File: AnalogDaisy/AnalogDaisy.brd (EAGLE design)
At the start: 58.1 x 43.2 mm, 21 parts, among them J1 1X2-3.5MM, J2 1X2-3.5MM, J3 1X2-3.5MM, J4 1X2-3.5MM, J5 1X2-3.5MM, J7 POWER_JACKPTH_BREAD, Q1 35A/25V/8.5mΩ, Q3 35A/25V/8.5mΩ, Q5 35A/25V/8.5mΩ, Q6 35A/25V/8.5mΩ

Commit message: moved inductor, git test
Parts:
- moved L1 24.1 mm to (8.89, 6.35)
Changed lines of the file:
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@@
 <?xml version="1.0" encoding="utf-8"?>
 <!DOCTYPE eagle SYSTEM "eagle.dtd">
-<eagle version="8.4.3">
+<eagle version="8.2.2">
 <drawing>
 <settings>
@@
 <param name="dpMaxLengthDifference" value="10mm"/>
 <param name="dpGapFactor" value="2.5"/>
+<param name="checkGrid" value="0"/>
 <param name="checkAngle" value="0"/>
 <param name="checkFont" value="1"/>
 <param name="checkRestrict" value="1"/>
-<param name="checkStop" value="0"/>
 <param name="useDiameter" value="13"/>
 <param name="maxErrors" value="50"/>
@@
 <element name="C12" library="microbuilder" package="0603-MINI" value="22uF 10V" x="6.35" y="-31.75"/>
 <element name="C13" library="microbuilder" package="0603-MINI" value="22uF 10V" x="-1.27" y="-34.29"/>
-<element name="L1" library="microbuilder" package="INDUCTOR_5X5MM_TDK_VLC5045" value="4.7uH" x="1.27" y="-16.51"/>
+<element name="L1" library="microbuilder" package="INDUCTOR_5X5MM_TDK_VLC5045" value="4.7uH" x="8.89" y="6.35"/>
 <element name="C14" library="microbuilder" package="0603-MINI" value="22nF" x="6.35" y="-34.29"/>
 <element name="D6" library="microbuilder" package="SOD-123" value="PMEG4030ER" x="-1.27" y="-27.94"/>
@@
 <contactref element="U$19" pad="P5"/>
 <wire x1="5.6" y1="-31.75" x2="-2.02" y2="-34.29" width="0" layer="19" extent="1-1"/>
-<wire x1="2.87" y1="-16.51" x2="5.6" y2="-31.75" width="0" layer="19" extent="1-1"/>
-<wire x1="6.87" y1="-12.88" x2="2.87" y2="-16.51" width="0" layer="19" extent="1-1"/>
+<wire x1="10.49" y1="6.35" x2="5.6" y2="-31.75" width="0" layer="19" extent="1-1"/>
+<wire x1="6.87" y1="-12.88" x2="10.49" y2="6.35" width="0" layer="19" extent="1-1"/>
 <wire x1="12.7" y1="12.7" x2="6.87" y2="-12.88" width="0" layer="19" extent="1-16"/>
 </signal>
@@
 <contactref element="U$19" pad="P13"/>
 <contactref element="D6" pad="C"/>
-<wire x1="-0.33" y1="-16.51" x2="-3.12" y2="-27.94" width="0" layer="19" extent="1-1"/>
-<wire x1="6.17" y1="-10.68" x2="-0.33" y2="-16.51" width="0" layer="19" extent="1-1"/>
+<wire x1="7.29" y1="6.35" x2="-3.12" y2="-27.94" width="0" layer="19" extent="1-1"/>
+<wire x1="6.17" y1="-10.68" x2="7.29" y2="6.35" width="0" layer="19" extent="1-1"/>
 <wire x1="6.87" y1="-9.98" x2="6.17" y2="-10.68" width="0" layer="19" extent="1-1"/>
 <wire x1="8.37" y1="-9.98" x2="6.87" y2="-9.98" width="0" layer="19" extent="1-1"/>
@@
 <compatibility>
 <note version="8.2" severity="warning">
-Since Version 8.2, EAGLE supports online libraries. The ids
+Since Version 8.2, Eagle supports online libraries. The ids
 of those online libraries will not be understood (or retained)
 with this version.

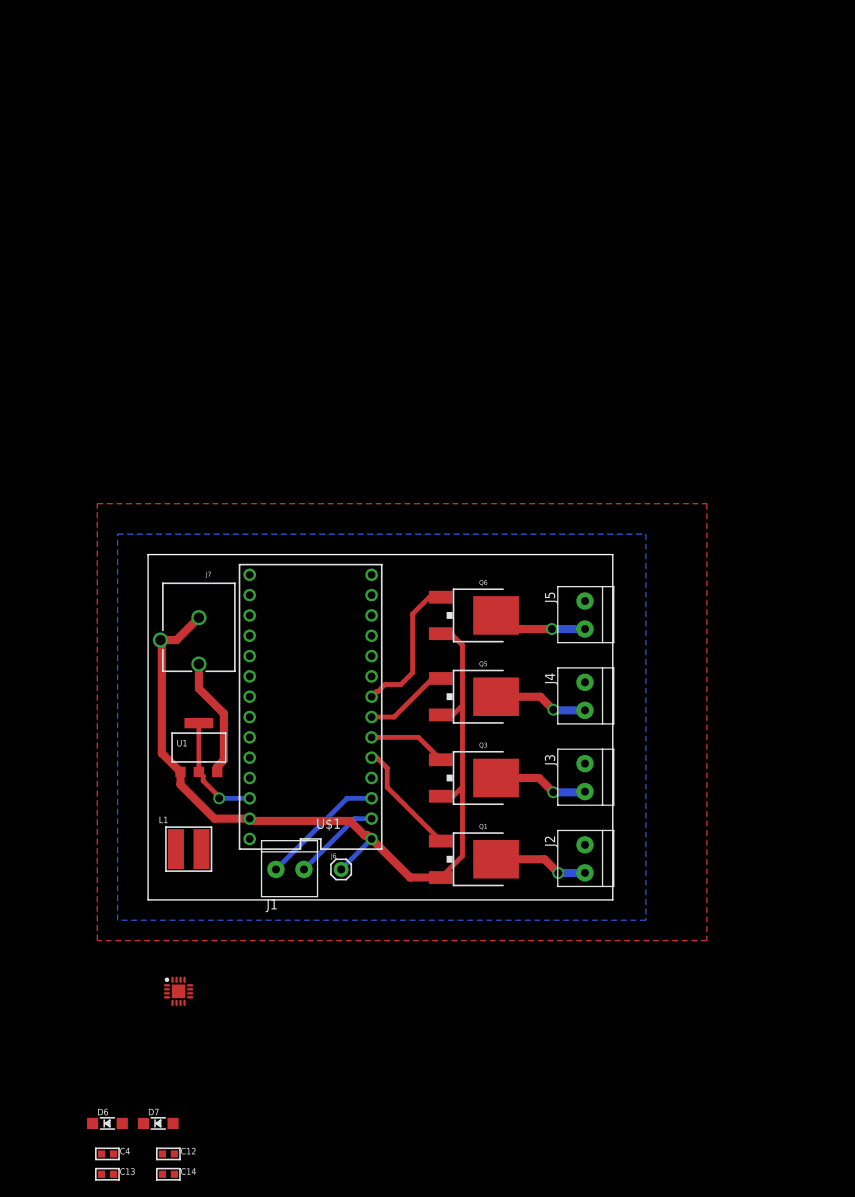
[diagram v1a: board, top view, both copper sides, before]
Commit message: Updated AnalogDaisy
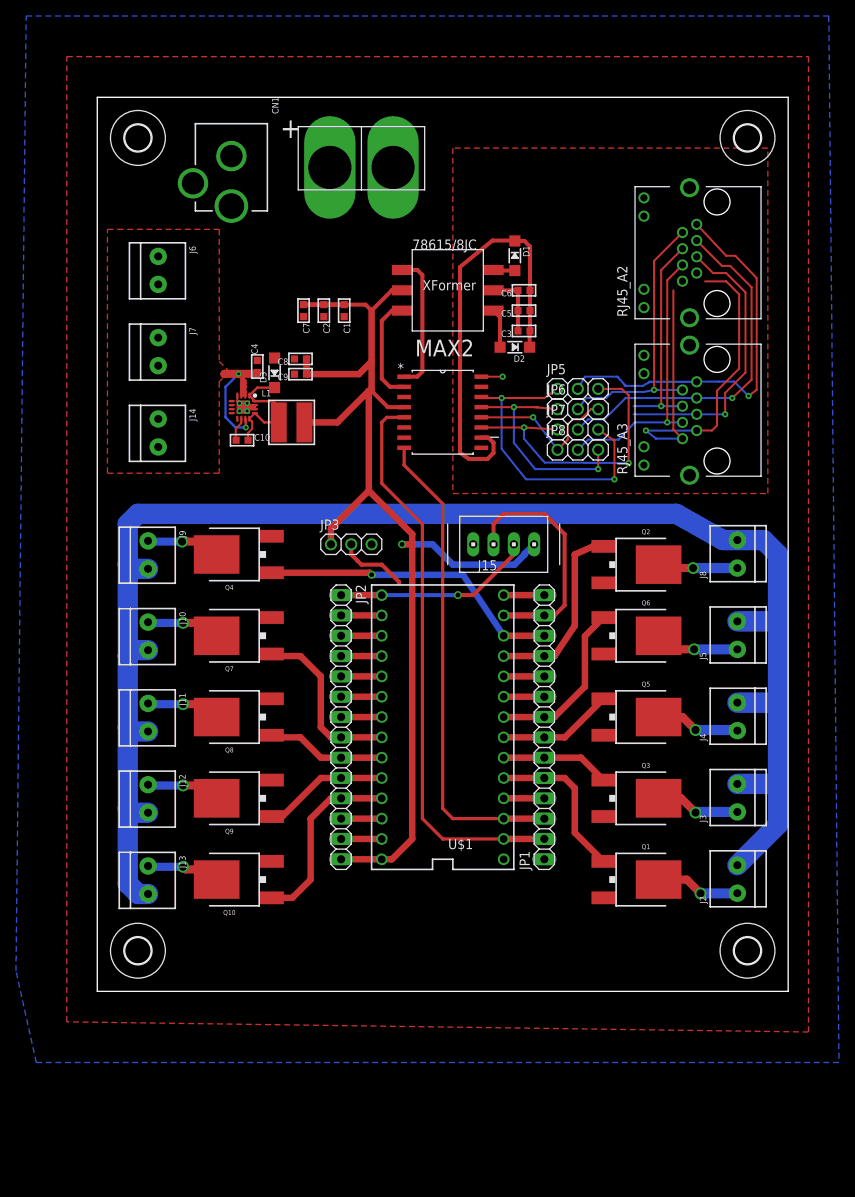
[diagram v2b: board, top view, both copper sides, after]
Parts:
- removed C12, C13: 22uF 10V, microbuilder:0603-MINI
- removed C14: 22nF, microbuilder:0603-MINI
- removed D6, D7: PMEG4030ER, microbuilder:SOD-123
- removed U1: (no value), microbuilder:SOT223-R
- added C1, C5: 1uF 10V, microbuilder:0603-MINI
- added C10: 22nF, microbuilder:0603-MINI
- added C2, C6: 0.1uF 10V, microbuilder:0603-MINI
- added C3, C7: 10uF 10V, microbuilder:0603-MINI
- added C8, C9: 22uF 10V, microbuilder:0603-MINI
- added CN1: (no value), microbuilder:DCJACK_2MM_PTH
- added D1, D2, D3: PMEG4030ER, microbuilder:SOD-123
- added J10, J11, J12, J13, J14, J8, J9: (no value), microbuilder:TERMBLOCK_1X2-3.5MM
- added J15: (no value), My Connectors:BOARDMOUNT-LED
- added JP1, JP2: (no value), adafruit:1X14
- added JP3, JP5, JP6, JP7, JP8: (no value), adafruit:1X03
- added MAX2: MAX14853GWE+, Maxim_By_element14_Batch_1:SOIC127P1034X267-16N
- added Q10, Q2, Q4, Q7, Q8, Q9: 35A/25V/8.5mΩ, SparkFun-DiscreteSemi:DPAK
- added RJ45_A2, RJ45_A3: RJHSE-5381, RJHSE-5381:AMPHENOL_RJHSE-5381
- added U$11, U$15, U$16: (no value), holes:3,3
- added U$2: BUCK_CONVERTER, Heep:QFN-16
- added XFORM2: 78615/8JC, trafo-murata:0.1_SMD
- J1: value 1X2-3.5MM -> POWERPOLE_POWER45A_DRILL; device adafruit:1X2-3.5MM -> powerpoles:POWERPOLE_PAIR_45A_HOLE
- J2, J3, J4, J5: value 1X2-3.5MM -> (none); device adafruit:1X2-3.5MM -> microbuilder:TERMBLOCK_1X2-3.5MM
- J6: device SparkFun-Connectors:1X01 -> microbuilder:TERMBLOCK_1X2-3.5MM
- J7: value POWER_JACKPTH_BREAD -> (none); device SparkFun-Connectors:POWER_JACK_PTH_BREAD -> microbuilder:TERMBLOCK_1X2-3.5MM
- U$19: value BUCK_CONVERTER -> (none); device Heep:QFN-16 -> holes:3,3
- moved C4 100.2 mm to (17.5, 66.7), turned to 90 degrees
- moved J1 89.3 mm to (30.5, 92.7), turned to 0 degrees
- moved J6 78.3 mm to (5.08, 78.7), turned to 270 degrees
- moved U$19 71.3 mm to (78.7, -6.35)
- moved L1 54.9 mm to (21.7, 59.7)
- moved J7 25.9 mm to (5.08, 68.6), turned to 270 degrees
- moved Q1 20.5 mm to (66.0, 2.54)
- moved Q3 20.5 mm to (66.0, 12.7)
- moved Q5 20.5 mm to (66.0, 22.9)
- moved Q6 20.5 mm to (66.0, 33.0)
- moved J2 19.2 mm to (77.5, 2.54)
- moved J3 19.2 mm to (77.5, 12.7)
- moved J4 19.2 mm to (77.5, 22.9)
- moved J5 19.2 mm to (77.5, 33.0)
- moved U$1 16.7 mm to (40.6, 21.6)
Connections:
- removed net +3V3: C12.1, C13.1, L1.P$2, U$1.3.3V, U$19.P5, U1.2, U1.4
- removed net VBUS: D7.A
- removed net VIN: U$1.VIN
- new net +3V1: U$2.P5
- new net +5V: C1.1, C2.1, C7.1, C9.1, J15.1, JP2.14, JP3.1, L1.P$2, MAX2.4, U$1.VIN, XFORM2.PIN2
- new net APA_CLOCK: J15.2, JP2.1, U$1.13
- new net APA_DATA: J15.3, JP1.13, U$1.11
- new net DRAIN10: J13.2, Q10.4
- new net DRAIN5: J8.2, Q2.4
- new net DRAIN6: J9.2, Q4.4
- new net DRAIN7: J10.2, Q7.4
- new net DRAIN8: J11.2, Q8.4
- new net DRAIN9: J12.2, Q9.4
- new net EN10: JP2.11, Q10.1, U$1.23/A9
- new net EN5: JP1.11, Q2.1, U$1.9
- new net EN6: JP1.12, Q4.1, U$1.10
- new net EN7: JP2.8, Q7.1, U$1.20/A6
- new net EN8: JP2.9, Q8.1, U$1.21/A7
- new net EN9: JP2.10, Q9.1, U$1.22/A8
- new net GNDB: C3.2, C5.2, C6.2, MAX2.15, MAX2.9, RJ45_A2.7, RJ45_A2.8, RJ45_A2.S1, RJ45_A2.S2, RJ45_A3.7, RJ45_A3.8, XFORM2.PIN5
- new net GNDBREAK: CN1.GNDBREAK
- new net N$10: JP1.14, U$1.12
- new net N$12: JP2.2, U$1.14/A0
- new net N$13: JP2.3, U$1.15/A1
- new net N$15: JP2.5, U$1.17/A3
- new net N$17: JP2.7, U$1.19/A5
- new net N$18: JP2.13, U$1.AGND
- new net N$3: JP2.12, U$1.3.3V
- new net N$4: C10.2, D3.C, L1.P$1, U$2.P1, U$2.P12, U$2.P13, U$2.P16
- new net N$5: D2.A, XFORM2.PIN4
- new net N$6: JP1.4, U$1.2
- new net N$7: JP1.9, U$1.7
- new net PWR: CN1.PWR
- new net RCV_EN: MAX2.6
- new net RJ45-1: JP5.2, RJ45_A2.1, RJ45_A3.1
- new net RJ45-2: JP6.2, RJ45_A2.2, RJ45_A3.2
- new net RJ45-3: JP7.2, RJ45_A2.3, RJ45_A3.3
- new net RJ45-4: RJ45_A2.4, RJ45_A3.4
- new net RJ45-5: RJ45_A2.5, RJ45_A3.5
- new net RJ45-6: JP8.2, RJ45_A2.6, RJ45_A3.6
- new net RX+: JP5.1, JP7.3, MAX2.14
- new net RX-: JP6.1, JP8.3, MAX2.13
- new net RXD: JP1.2, MAX2.5, U$1.0
- new net SEND_EN: MAX2.7
- new net TD1: MAX2.1, XFORM2.PIN1
- new net TD2: MAX2.2, XFORM2.PIN3
- new net TX+: JP5.3, JP7.1, MAX2.11
- new net TX-: JP6.3, JP8.1, MAX2.12
- new net TXD: JP1.3, MAX2.8, U$1.1
- new net V+: J1.RED
- new net VCCB: MAX2.16
- new net VLDO: C3.1, C5.1, C6.1, D1.C, D2.C, MAX2.10
- new net WS2812_DATA: JP1.10, JP3.2, U$1.8
- net EN1: now also JP1.5
- net EN2: now also JP1.6
- net EN3: now also JP1.7
- net EN4: now also JP1.8
- net GND: now also C1.2, C2.2, C7.2, C8.2, C9.2, CN1.GND, D3.A, J1.BLACK, J14.2, J15.4, J6.2, J7.2, JP1.1, JP3.3, MAX2.3, Q10.3, Q2.3, Q4.3, Q7.3, Q8.3, Q9.3, U$2.P14, U$2.P15, U$2.P4, U$2.PAD; no longer C12.2, C13.2, D6.A, J6.1, J7.GND, J7.GNDBREAK, U$1.AGND, U$19.P14, U$19.P15, U$19.P4, U$19.PAD, U1.1
- net N$1: now also C10.1, U$2.P10; no longer J1.1, U$1.1
- net N$14: now also JP2.4, U$1.16/A2; no longer C14.1, U$19.P10
- net N$16: now also JP2.6, U$1.18/A4; no longer C14.2, D6.C, L1.P$1, U$19.P1, U$19.P12, U$19.P13, U$19.P16
- net N$2: now also D1.A, XFORM2.PIN6; no longer J1.2, U$1.0
- net VBAT: now also J10.1, J11.1, J12.1, J13.1, J8.1, J9.1, U$2.P11, U$2.P2, U$2.P3; no longer D7.C, J7.PWR, U$19.P11, U$19.P2, U$19.P3, U1.3
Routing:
- net VBAT: track 15.1 -> 224.8 mm, vias 0 -> 2
- net +5V: track 0.00 -> 151.2 mm, vias 0 -> 1
- net GND: track 107.7 -> 6.54 mm, vias 0 -> 4
- net RXD: track 0.00 -> 71.0 mm
- net GNDB: track 0.00 -> 63.7 mm, vias 0 -> 1
- net TXD: track 0.00 -> 60.3 mm
- net VLDO: track 0.00 -> 53.9 mm
- net RJ45-1: track 0.00 -> 49.5 mm, vias 0 -> 1
- net RJ45-3: track 0.00 -> 45.1 mm, vias 0 -> 1
- net RX+: track 0.00 -> 39.5 mm, vias 0 -> 2
- net TX+: track 0.00 -> 38.4 mm, vias 0 -> 2
- net EN6: track 0.00 -> 38.2 mm, vias 0 -> 1
- net RJ45-5: track 0.00 -> 35.7 mm, vias 0 -> 1
- net RJ45-2: track 0.00 -> 35.3 mm, vias 0 -> 1
- net RJ45-6: track 0.00 -> 35.0 mm, vias 0 -> 1
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- added copper zone on layer 16, net GND
- added copper zone on layer 1, net GNDB
- added copper zone on layer 1, net VBAT
- removed copper zone on layer 16, net VBAT
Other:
- board size 58.1 x 43.2 mm -> 86.4 x 111.8 mm

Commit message: Updated AnalogDaisy Wiring
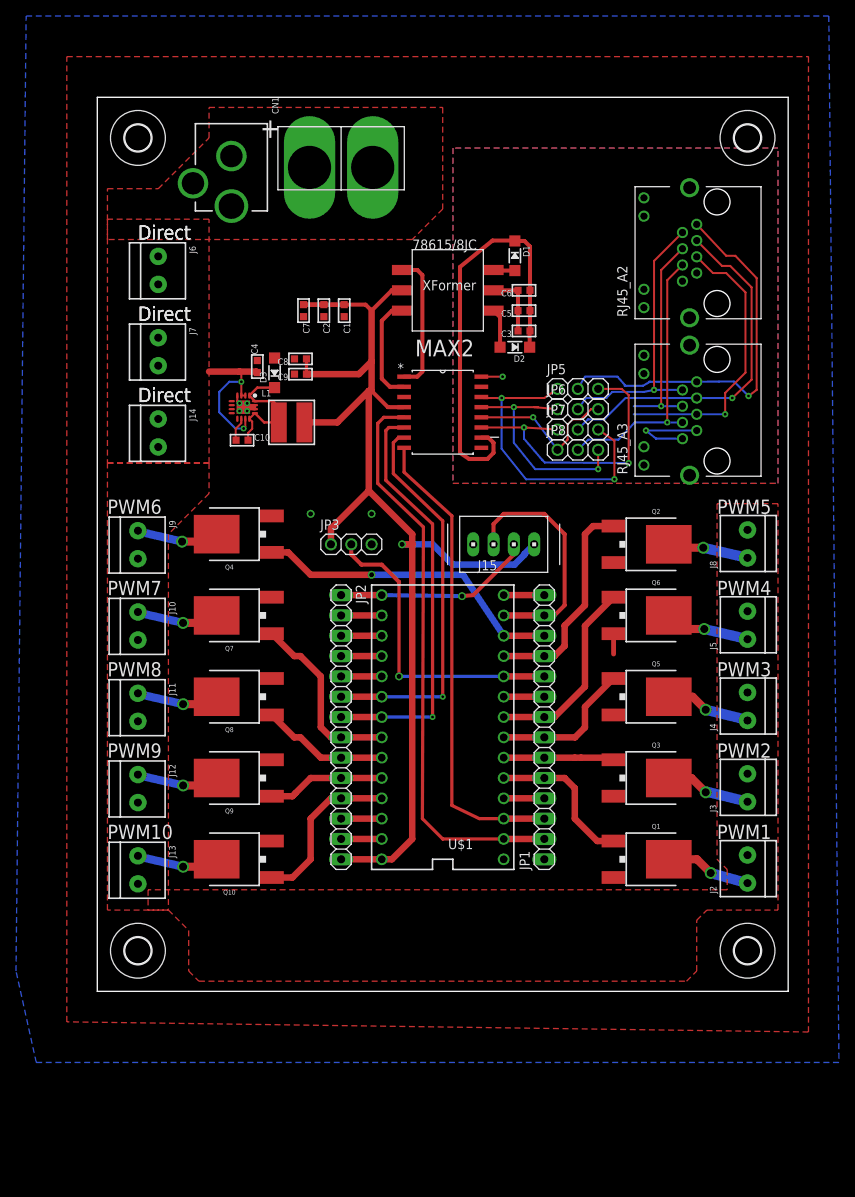
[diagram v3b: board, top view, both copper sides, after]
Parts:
- moved Q2 2.84 mm to (67.3, 44.5)
- moved Q3 2.84 mm to (67.3, 15.2)
- moved Q1 2.84 mm to (67.3, 5.08)
- moved Q5 2.84 mm to (67.3, 25.4)
- moved Q6 2.84 mm to (67.3, 35.6)
- moved Q9 2.54 mm to (14.0, 15.2)
- moved Q10 2.54 mm to (14.0, 5.08)
- moved J1 2.54 mm to (27.9, 92.7)
- moved Q4 2.54 mm to (14.0, 45.7)
- moved Q7 2.54 mm to (14.0, 35.6)
- moved Q8 2.54 mm to (14.0, 25.4)
- moved J9 1.80 mm to (2.54, 44.5)
- moved J12 1.80 mm to (2.54, 14.0)
- moved J13 1.80 mm to (2.54, 3.81)
- moved J11 1.80 mm to (2.54, 24.1)
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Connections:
- removed net GNDBREAK: CN1.GNDBREAK
- removed net N$16: JP2.6, U$1.18/A4
- removed net N$17: JP2.7, U$1.19/A5
- removed net PWR: CN1.PWR
- removed net V+: J1.RED
- net +5V: now also C8.1
- net GND: now also CN1.GNDBREAK
- net RCV_EN: now also JP2.7, U$1.19/A5
- net SEND_EN: now also JP2.6, U$1.18/A4
- net VBAT: now also CN1.PWR, J1.RED
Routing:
- net VBAT: track 224.8 -> 20.7 mm
- net RCV_EN: track 0.00 -> 52.2 mm, vias 0 -> 1
- net SEND_EN: track 0.00 -> 48.7 mm, vias 0 -> 1
- net GNDB: track 63.7 -> 19.4 mm
- net WS2812_DATA: track 13.9 -> 38.6 mm, vias 0 -> 1
- net N$17: track 5.08 -> 0.00 mm
- net N$16: track 5.08 -> 0.00 mm
- net EN3: track 14.5 -> 18.3 mm
- net EN5: track 23.6 -> 27.2 mm
- net GND: track 6.54 -> 9.88 mm, vias 4 -> 6
- net EN4: track 21.3 -> 24.4 mm
- net EN10: track 23.4 -> 20.8 mm
- net DRAIN9: track 14.5 -> 12.3 mm
- net DRAIN10: track 12.3 -> 14.4 mm
- net DRAIN6: track 9.46 -> 11.4 mm
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- added copper zone on layer 16, net GNDB
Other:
- board text added: "Direct"
- board text added: "PWM1"
- board text added: "PWM10"
- board text added: "PWM2"
- board text added: "PWM3"
- board text added: "PWM4"
- board text added: "PWM5"
- board text added: "PWM6"
- board text added: "PWM7"
- board text added: "PWM8"
- board text added: "PWM9"
